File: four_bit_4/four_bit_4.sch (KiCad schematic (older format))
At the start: 1 part, among them P1 DIN_41612_128P

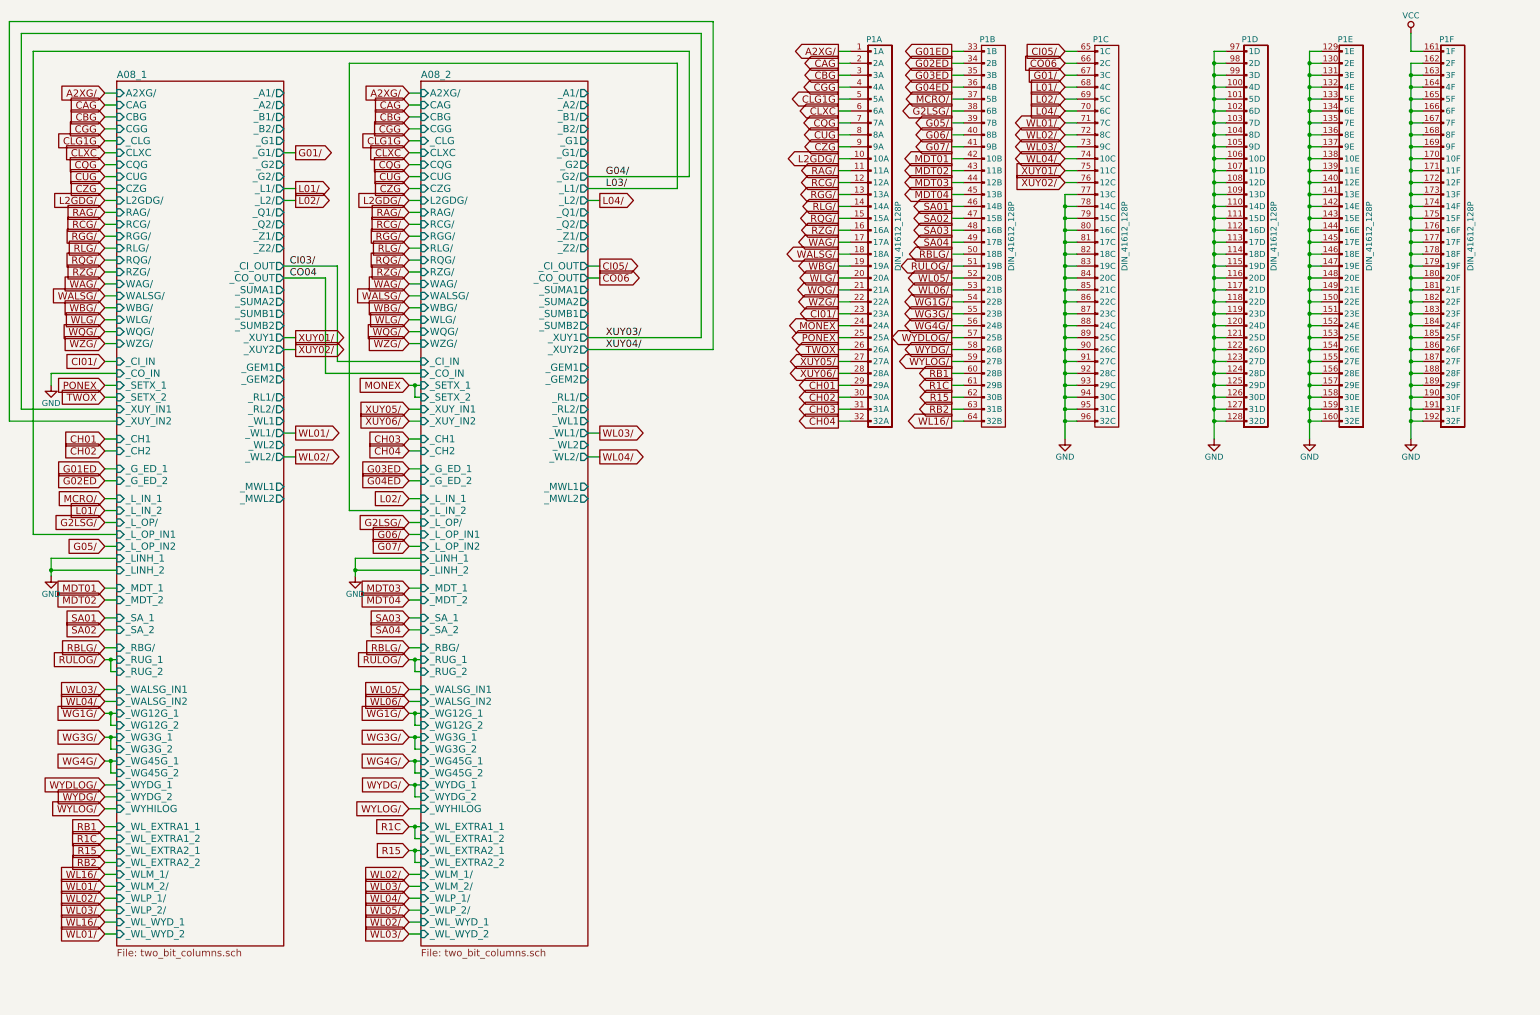
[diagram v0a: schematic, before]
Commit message: Added the final four bit module. All 16 bits of the central/special registers are present. We're stuck at address 0 because TC is using RAD, which needs to be translated into RG or RZ by module 12
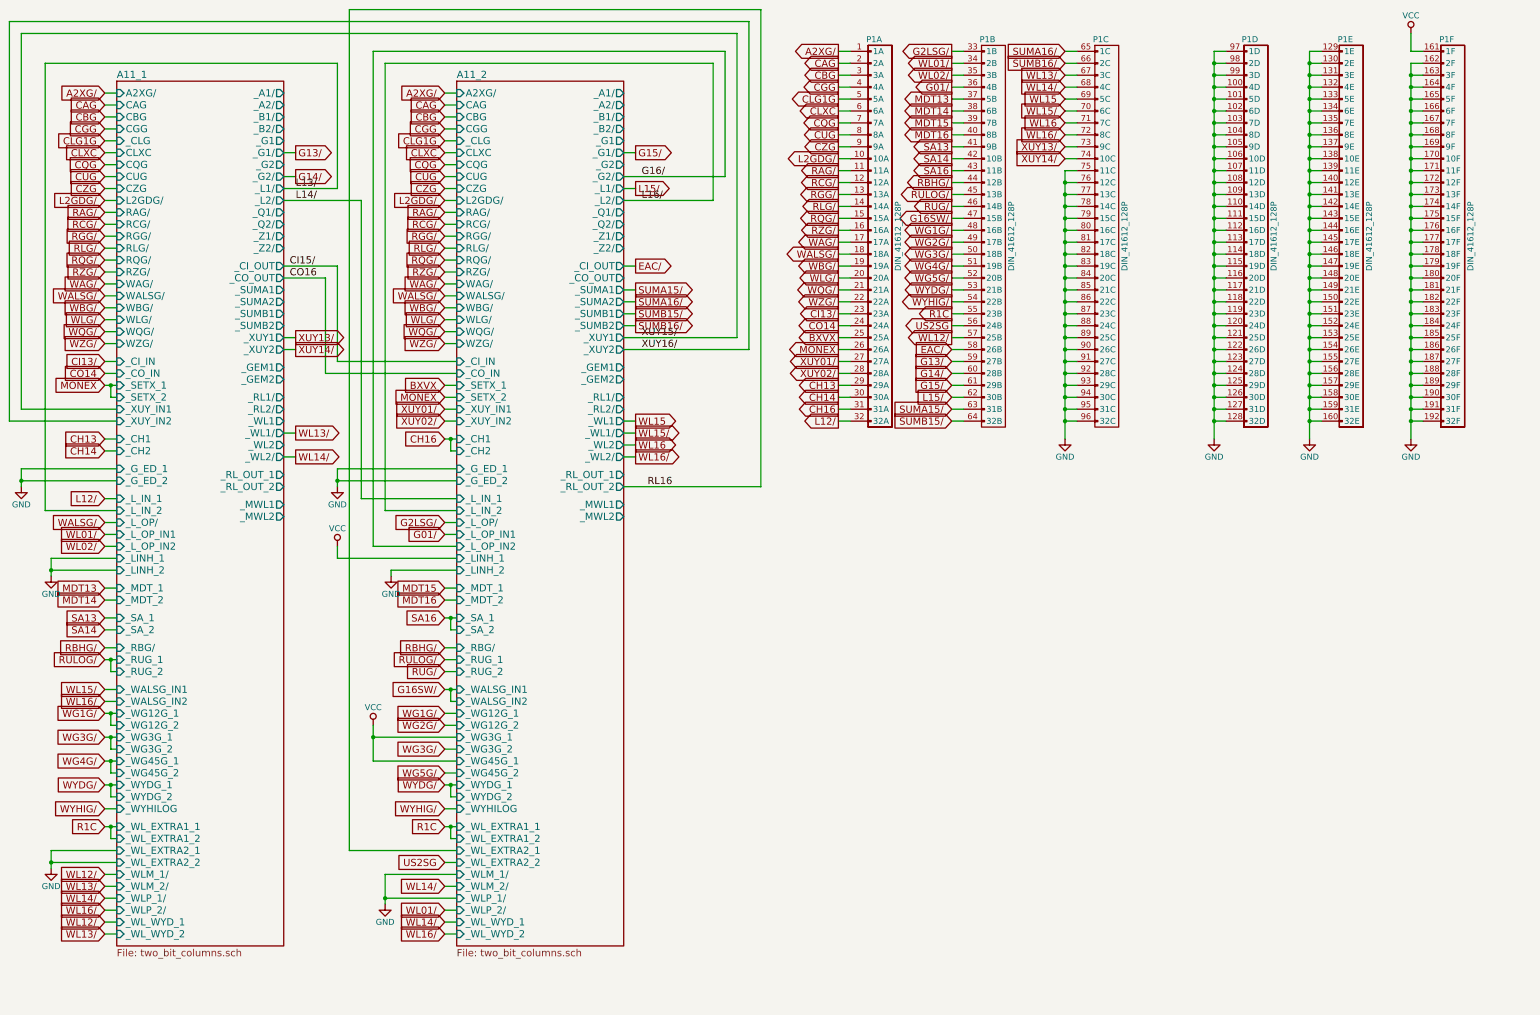
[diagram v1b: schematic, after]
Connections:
- net G01ED is gone; now on net G2LSG/: P1.33 (1B)
- net G02ED is gone; now on net WL01/: P1.34 (2B)
- net G03ED is gone; now on net WL02/: P1.35 (3B)
- net G04ED is gone; now on net G01/: P1.36 (4B)
- net MDT04 is gone; now on net RULOG/: P1.45 (13B)
- net RBLG/ is gone; now on net WG3G/: P1.50 (18B)
- net SA03 is gone; now on net WG1G/: P1.48 (16B)
- net TWOX is gone; now on net MONEX: P1.26 (26A)
- net WL06/ is gone; now on net WYDG/: P1.53 (21B)
- net XUY05/ is gone; now on net XUY01/: P1.27 (27A)
- net XUY06/ is gone; now on net XUY02/: P1.28 (28A)
- net G01/: no longer P1.67 (3C)
- net G2LSG/: no longer P1.38 (6B)
- net GND: now also P1.75 (11C), P1.76 (12C)
- net MONEX: no longer P1.24 (24A)
- net R1C: now also P1.55 (23B); no longer P1.61 (29B)
- net RULOG/: no longer P1.51 (19B)
- net WG1G/: no longer P1.54 (22B)
- net WG3G/: no longer P1.55 (23B)
- net WG4G/: now also P1.51 (19B); no longer P1.56 (24B)
- net WL01/: no longer P1.71 (7C)
- net WL02/: no longer P1.72 (8C)
- net WL16/: now also P1.72 (8C); no longer P1.64 (32B)
- net WYDG/: no longer P1.58 (26B)
- net XUY01/: no longer P1.75 (11C)
- net XUY02/: no longer P1.76 (12C)
- net CH01 renamed CH13
- net CH02 renamed CH14
- net CH03 renamed CH16
- net CH04 renamed L12/
- net CI01/ renamed CI13/
- net CI05/ renamed SUMA16/
- net CO06 renamed SUMB16/
- net G05/ renamed MDT15
- net G06/ renamed MDT16
- net G07/ renamed SA13
- net L01/ renamed WL14/
- net L02/ renamed WL15
- net L04/ renamed WL15/
- net MCRO/ renamed MDT13
- net MDT01 renamed SA14
- net MDT02 renamed SA16
- net MDT03 renamed RBHG/
- net PONEX renamed BXVX
- net R15 renamed L15/
- net RB1 renamed G14/
- net RB2 renamed SUMA15/
- net SA01 renamed RUG/
- net SA02 renamed G16SW/
- net SA04 renamed WG2G/
- net WL03/ renamed XUY13/
- net WL04/ renamed XUY14/
- net WL05/ renamed WG5G/
- net WYDLOG/ renamed WL12/
- net WYLOG/ renamed G13/
- new net CO14: P1.24 (24A)
- new net EAC/: P1.58 (26B)
- new net G15/: P1.61 (29B)
- new net MDT14: P1.38 (6B)
- new net SUMB15/: P1.64 (32B)
- new net US2SG: P1.56 (24B)
- new net WL13/: P1.67 (3C)
- new net WL16: P1.71 (7C)
- new net WYHIG/: P1.54 (22B)

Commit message: Added in WHOMP, whatever it is
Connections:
- net EAC/: now also P1.59 (27B); no longer P1.58 (26B)
- net G13/: now also P1.60 (28B); no longer P1.59 (27B)
- net G14/: now also P1.61 (29B); no longer P1.60 (28B)
- net G15/: now also P1.62 (30B); no longer P1.61 (29B)
- net GND: no longer P1.75 (11C)
- net L15/: now also P1.63 (31B); no longer P1.62 (30B)
- net SUMA15/: now also P1.64 (32B); no longer P1.63 (31B)
- net SUMA16/: now also P1.66 (2C); no longer P1.65 (1C)
- net SUMB15/: now also P1.65 (1C); no longer P1.64 (32B)
- net SUMB16/: now also P1.67 (3C); no longer P1.66 (2C)
- net WL13/: now also P1.68 (4C); no longer P1.67 (3C)
- net WL14/: now also P1.69 (5C); no longer P1.68 (4C)
- net WL15: now also P1.70 (6C); no longer P1.69 (5C)
- net WL15/: now also P1.71 (7C); no longer P1.70 (6C)
- net WL16: now also P1.72 (8C); no longer P1.71 (7C)
- net WL16/: now also P1.73 (9C); no longer P1.72 (8C)
- net XUY13/: now also P1.74 (10C); no longer P1.73 (9C)
- net XUY14/: now also P1.75 (11C); no longer P1.74 (10C)
- new net WHOMPA: P1.58 (26B)
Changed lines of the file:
@@
 $EndDescr
 $Sheet
-S 1750 1200 1400 7250
+S 1750 1200 1400 7600
 U 568CD527
 F0 "A11_1" 60
@@
 F101 "_RL_OUT_2" O R 3150 4600 60
 F102 "_RL_OUT_1" O R 3150 4500 60
+F103 "_WHOMPA" I L 1750 8700 60
+F104 "_WHOMP_1" I L 1750 8500 60
+F105 "_WHOMP_2" I L 1750 8600 60
 $EndSheet
 $Comp
@@
 $EndComp
 $Sheet
-S 4600 1200 1400 7250
+S 4600 1200 1400 7600
 U 568CD532
 F0 "A11_2" 60
@@
 F101 "_RL_OUT_2" O R 6000 4600 60
 F102 "_RL_OUT_1" O R 6000 4500 60
+F103 "_WHOMPA" I L 4600 8700 60
+F104 "_WHOMP_1" I L 4600 8500 60
+F105 "_WHOMP_2" I L 4600 8600 60
 $EndSheet
 Text GLabel 1650 1300 0    60   Input ~ 0
@@
 	4600 8350 4500 8350
 Wire Wire Line
-	9700 1950 9800 1950
-Wire Wire Line
 	9700 2050 9800 2050
-Connection ~ 9700 2050
 Wire Wire Line
 	9700 2150 9800 2150
@@
 Wire Wire Line
 	6000 1800 6100 1800
-Text GLabel 8750 3550 0    60   Input ~ 0
+Text GLabel 8750 3650 0    60   Input ~ 0
 G13/
-Wire Wire Line
-	8850 3550 8750 3550
-Text GLabel 8750 3650 0    60   Input ~ 0
-G14/
 Wire Wire Line
 	8850 3650 8750 3650
 Text GLabel 8750 3750 0    60   Input ~ 0
+G14/
+Wire Wire Line
+	8850 3750 8750 3750
+Text GLabel 8750 3850 0    60   Input ~ 0
 G15/
 Wire Wire Line
-	8850 3750 8750 3750
+	8850 3850 8750 3850
 Text GLabel 6100 2100 2    60   Output ~ 0
 L15/
 Wire Wire Line
 	6000 2100 6100 2100
-Text GLabel 8750 3850 0    60   Input ~ 0
+Text GLabel 8750 3950 0    60   Input ~ 0
 L15/
 Wire Wire Line
-	8850 3850 8750 3850
+	8850 3950 8750 3950
 Text GLabel 6100 3050 2    60   Output ~ 0
 SUMA16/
@@
 Wire Wire Line
 	6000 3250 6100 3250
-Text GLabel 9700 950  0    60   Input ~ 0
+Text GLabel 9700 1050 0    60   Input ~ 0
 SUMA16/
 Wire Wire Line
-	9800 950  9700 950
-Text GLabel 9700 1050 0    60   Input ~ 0
+	9800 1050 9700 1050
+Text GLabel 9700 1150 0    60   Input ~ 0
 SUMB16/
 Wire Wire Line
-	9800 1050 9700 1050
+	9800 1150 9700 1150
 Text GLabel 3250 3350 2    60   Output ~ 0
 XUY13/
@@
 Wire Wire Line
 	3150 3450 3250 3450
-Text GLabel 9700 1750 0    60   Input ~ 0
+Text GLabel 9700 1850 0    60   Input ~ 0
 XUY13/
 Wire Wire Line
-	9800 1750 9700 1750
-Text GLabel 9700 1850 0    60   Input ~ 0
+	9800 1850 9700 1850
+Text GLabel 9700 1950 0    60   Input ~ 0
 XUY14/
 Wire Wire Line
-	9800 1850 9700 1850
+	9800 1950 9700 1950
 Text GLabel 6100 4050 2    60   Output ~ 0
 WL15
@@
 Wire Wire Line
 	6000 4250 6100 4250
-Text GLabel 9700 1150 0    60   Input ~ 0
+Text GLabel 9700 1250 0    60   Input ~ 0
 WL13/
-Text GLabel 9700 1250 0    60   Input ~ 0
+Text GLabel 9700 1350 0    60   Input ~ 0
 WL14/
 Wire Wire Line
-	9800 1150 9700 1150
-Wire Wire Line
 	9800 1250 9700 1250
+Wire Wire Line
+	9800 1350 9700 1350
+Text GLabel 9700 1550 0    60   Input ~ 0
+WL15/
+Wire Wire Line
+	9800 1550 9700 1550
+Wire Wire Line
+	9800 1750 9700 1750
 Text GLabel 9700 1450 0    60   Input ~ 0
-WL15/
+WL15
+Text GLabel 9700 1650 0    60   Input ~ 0
+WL16
 Wire Wire Line
 	9800 1450 9700 1450
 Wire Wire Line
 	9800 1650 9700 1650
-Text GLabel 9700 1350 0    60   Input ~ 0
-WL15
-Text GLabel 9700 1550 0    60   Input ~ 0
-WL16
-Wire Wire Line
-	9800 1350 9700 1350
-Wire Wire Line
-	9800 1550 9700 1550
-Text GLabel 9700 1650 0    60   Input ~ 0
+Text GLabel 9700 1750 0    60   Input ~ 0
 WL16/
 Wire Wire Line
-	9700 1950 9700 4200
+	9700 2050 9700 4200
 Text GLabel 6100 2750 2    60   Output ~ 0
 EAC/
 Wire Wire Line
 	6000 2750 6100 2750
-Text GLabel 8750 3450 0    60   Input ~ 0
+Text GLabel 8750 3550 0    60   Input ~ 0
 EAC/
 Wire Wire Line
-	8850 3450 8750 3450
+	8850 3550 8750 3550
 Text GLabel 6100 2950 2    60   Output ~ 0
 SUMA15/
@@
 Wire Wire Line
 	6000 2950 6100 2950
-Text GLabel 8750 3950 0    60   Input ~ 0
+Text GLabel 8750 4050 0    60   Input ~ 0
 SUMA15/
 Wire Wire Line
-	8850 3950 8750 3950
-Text GLabel 8750 4050 0    60   Input ~ 0
+	8850 4050 8750 4050
+Text GLabel 9700 950  0    60   Input ~ 0
 SUMB15/
 Wire Wire Line
-	8850 4050 8750 4050
+	9800 950  9700 950
+$Comp
+L GND #PWR014
+U 1 1 56D0A797
+P 1200 8750
+F 0 "#PWR014" H 1200 8500 50  0001 C CNN
+F 1 "GND" H 1200 8600 50  0000 C CNN
+F 2 "" H 1200 8750 60  0000 C CNN
+F 3 "" H 1200 8750 60  0000 C CNN
+	1    1200 8750
+	1    0    0    -1
+$EndComp
+Wire Wire Line
+	1750 8600 1200 8600
+Wire Wire Line
+	1200 8500 1200 8750
+Wire Wire Line
+	1750 8700 1200 8700
+Connection ~ 1200 8700
+Wire Wire Line
+	1200 8500 1750 8500
+Connection ~ 1200 8600
+$Comp
+L GND #PWR015
+U 1 1 56D0AEA5
+P 3950 8750
+F 0 "#PWR015" H 3950 8500 50  0001 C CNN
+F 1 "GND" H 3950 8600 50  0000 C CNN
+F 2 "" H 3950 8750 60  0000 C CNN
+F 3 "" H 3950 8750 60  0000 C CNN
+	1    3950 8750
+	1    0    0    -1
+$EndComp
+Wire Wire Line
+	3950 8500 3950 8750
+Wire Wire Line
+	4600 8700 3950 8700
+Connection ~ 3950 8700
+Wire Wire Line
+	3950 8500 4600 8500
+Text GLabel 4500 8600 0    60   Input ~ 0
+WHOMPA
+Wire Wire Line
+	4600 8600 4500 8600
+Text GLabel 8750 3450 0    60   Output ~ 0
+WHOMPA
+Wire Wire Line
+	8850 3450 8750 3450
 $EndSCHEMATC

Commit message: Added and tied in module 12, parity & s register
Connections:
- net BXVX: now also P1.26 (26A); no longer P1.25 (25A)
- net CH13: now also P1.30 (30A); no longer P1.29 (29A)
- net CH14: now also P1.31 (31A); no longer P1.30 (30A)
- net CH16: now also P1.32 (32A); no longer P1.31 (31A)
- net CI13/: now also P1.24 (24A); no longer P1.23 (23A)
- net CLXC: now also P1.7 (7A); no longer P1.6 (6A)
- net CO14: now also P1.25 (25A); no longer P1.24 (24A)
- net CQG: now also P1.8 (8A); no longer P1.7 (7A)
- net CUG: now also P1.9 (9A); no longer P1.8 (8A)
- net CZG: now also P1.10 (10A); no longer P1.9 (9A)
- net EAC/: now also P1.60 (28B); no longer P1.59 (27B)
- net G01/: now also P1.37 (5B); no longer P1.36 (4B)
- net G13/: now also P1.62 (30B); no longer P1.60 (28B)
- net G14/: now also P1.64 (32B); no longer P1.61 (29B)
- net G15/: now also P1.66 (2C); no longer P1.62 (30B)
- net G16SW/: now also P1.48 (16B); no longer P1.47 (15B)
- net G2LSG/: now also P1.34 (2B); no longer P1.33 (1B)
- net GND: no longer P1.76 (12C), P1.77 (13C), P1.78 (14C), P1.79 (15C), P1.80 (16C)
- net L12/: now also P1.33 (1B); no longer P1.32 (32A)
- net L15/: now also P1.68 (4C); no longer P1.63 (31B)
- net L2GDG/: now also P1.11 (11A); no longer P1.10 (10A)
- net MDT13: now also P1.38 (6B); no longer P1.37 (5B)
- net MDT14: now also P1.39 (7B); no longer P1.38 (6B)
- net MDT15: now also P1.40 (8B); no longer P1.39 (7B)
- net MDT16: now also P1.41 (9B); no longer P1.40 (8B)
- net MONEX: now also P1.27 (27A); no longer P1.26 (26A)
- net R1C: now also P1.56 (24B); no longer P1.55 (23B)
- net RAG/: now also P1.12 (12A); no longer P1.11 (11A)
- net RBHG/: now also P1.45 (13B); no longer P1.44 (12B)
- net RCG/: now also P1.13 (13A); no longer P1.12 (12A)
- net RGG/: now also P1.14 (14A); no longer P1.13 (13A)
- net RLG/: now also P1.15 (15A); no longer P1.14 (14A)
- net RQG/: now also P1.16 (16A); no longer P1.15 (15A)
- net RUG/: now also P1.47 (15B); no longer P1.46 (14B)
- net RULOG/: now also P1.46 (14B); no longer P1.45 (13B)
- net RZG/: now also P1.17 (17A); no longer P1.16 (16A)
- net SA13: now also P1.42 (10B); no longer P1.41 (9B)
- net SA14: now also P1.43 (11B); no longer P1.42 (10B)
- net SA16: now also P1.44 (12B); no longer P1.43 (11B)
- net SUMA15/: now also P1.69 (5C); no longer P1.64 (32B)
- net SUMA16/: now also P1.71 (7C); no longer P1.66 (2C)
- net SUMB15/: now also P1.70 (6C); no longer P1.65 (1C)
- net SUMB16/: now also P1.72 (8C); no longer P1.67 (3C)
- net US2SG: now also P1.57 (25B); no longer P1.56 (24B)
- net WAG/: now also P1.18 (18A); no longer P1.17 (17A)
- net WALSG/: now also P1.19 (19A); no longer P1.18 (18A)
- net WBG/: now also P1.20 (20A); no longer P1.19 (19A)
- net WG1G/: now also P1.49 (17B); no longer P1.48 (16B)
- net WG2G/: now also P1.50 (18B); no longer P1.49 (17B)
- net WG3G/: now also P1.51 (19B); no longer P1.50 (18B)
- net WG4G/: now also P1.52 (20B); no longer P1.51 (19B)
- net WG5G/: now also P1.53 (21B); no longer P1.52 (20B)
- net WHOMPA: now also P1.59 (27B); no longer P1.58 (26B)
- net WL01/: now also P1.35 (3B); no longer P1.34 (2B)
- net WL02/: now also P1.36 (4B); no longer P1.35 (3B)
- net WL12/: now also P1.58 (26B); no longer P1.57 (25B)
- net WL13/: now also P1.73 (9C); no longer P1.68 (4C)
- net WL14/: now also P1.74 (10C); no longer P1.69 (5C)
- net WL15: now also P1.75 (11C); no longer P1.70 (6C)
- net WL15/: now also P1.76 (12C); no longer P1.71 (7C)
- net WL16: now also P1.77 (13C); no longer P1.72 (8C)
- net WL16/: now also P1.78 (14C); no longer P1.73 (9C)
- net WLG/: now also P1.21 (21A); no longer P1.20 (20A)
- net WQG/: now also P1.22 (22A); no longer P1.21 (21A)
- net WYDG/: now also P1.54 (22B); no longer P1.53 (21B)
- net WYHIG/: now also P1.55 (23B); no longer P1.54 (22B)
- net WZG/: now also P1.23 (23A); no longer P1.22 (22A)
- net XUY01/: now also P1.28 (28A); no longer P1.27 (27A)
- net XUY02/: now also P1.29 (29A); no longer P1.28 (28A)
- net XUY13/: now also P1.79 (15C); no longer P1.74 (10C)
- net XUY14/: now also P1.80 (16C); no longer P1.75 (11C)
- new net CLG2G: P1.6 (6A)
- new net G13: P1.61 (29B)
- new net G14: P1.63 (31B)
- new net G15: P1.65 (1C)
- new net G16: P1.67 (3C)
